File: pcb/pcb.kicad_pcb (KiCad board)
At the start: 2 copper layers, 62 parts, among them CN10 1x2, CN11 1x6, CN2 1x8, CN3 1x8, CN4 1x8, CN7 1x2, CN9 2x5, IC1 AP2112K-3.3TRG1, IC2 STM32f103C8T, IC4 AP62300TWU-7, SW1 switch_3x4, SW2 switch_3x4

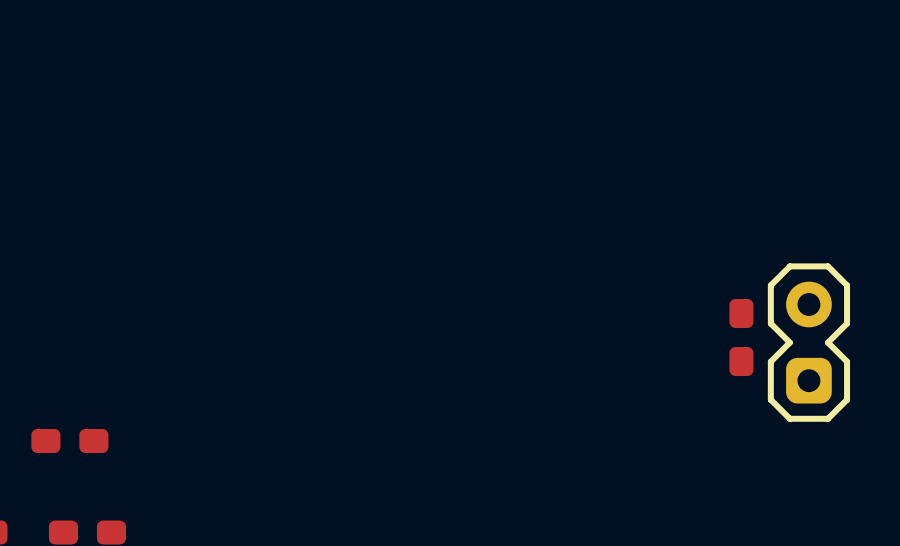
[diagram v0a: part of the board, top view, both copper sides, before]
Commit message: fixed 5V being GND net
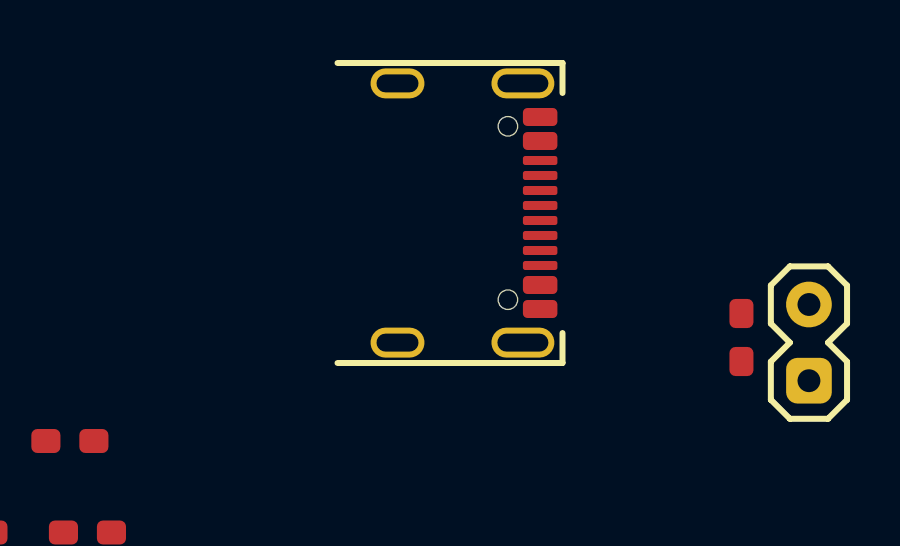
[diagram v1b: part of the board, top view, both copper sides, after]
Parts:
- added CN8: ~, USB:USB4105-GF-A, F.Cu at (121.3, 85.8)
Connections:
- C1 pad 1: GND -> 5V
- C24 pad 1: GND -> 5V
- C4 pad 1: GND -> 5V
- C5 pad 1: GND -> 5V
- C6 pad 1: GND -> 5V
- CN7 pad 1: GND -> 5V
- IC1 pad 1: GND -> 5V
- IC1 pad 3: GND -> 5V
- R8 pad 2: GND -> 5V
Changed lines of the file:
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@@
   (net 62 "unconnected-(CN9-Pad7)")
   (net 63 "/CAN_L")
+  (net 64 "5V")
+  (net 65 "unconnected-(CN8-SBU1-PadA8)")
+  (net 66 "unconnected-(CN8-SBU2-PadB8)")
   (footprint "pin_headers:1x2" (layer "F.Cu")
     (at 135 88.9 180)
@@
       (stroke (width 0.2) (type solid)) (layer "F.SilkS"))
     (pad "1" thru_hole roundrect (at 0 -2.54 90) (size 1.524 1.524) (drill 0.762) (layers "*.Cu" "*.Mask") (roundrect_rratio 0.25)
-      (net 1 "GND") (pintype "bidirectional"))
+      (net 64 "5V") (pintype "bidirectional"))
     (pad "2" thru_hole circle (at 0 0 90) (size 1.524 1.524) (drill 0.762) (layers "*.Cu" "*.Mask")
       (net 61 "/Servo VCC") (pintype "bidirectional"))
@@
       (net 4 "Net-(IC4-FB)") (pintype "bidirectional"))
     (pad "2" smd roundrect (at 0.8 0 180) (size 0.97 0.8) (layers "F.Cu" "F.Paste" "F.Mask") (roundrect_rratio 0.25)
-      (net 1 "GND") (pintype "bidirectional"))
+      (net 64 "5V") (pintype "bidirectional"))
   )
   (footprint "SMT:0603" (layer "F.Cu")
@@
       (stroke (width 0.2) (type solid)) (layer "F.Fab"))
     (pad "1" smd roundrect (at -0.8 0 90) (size 0.97 0.8) (layers "F.Cu" "F.Paste" "F.Mask") (roundrect_rratio 0.25)
-      (net 1 "GND") (pintype "bidirectional"))
+      (net 64 "5V") (pintype "bidirectional"))
     (pad "2" smd roundrect (at 0.8 0 90) (size 0.97 0.8) (layers "F.Cu" "F.Paste" "F.Mask") (roundrect_rratio 0.25)
       (net 1 "GND") (pintype "bidirectional"))
@@
       (net 1 "GND") (pintype "bidirectional"))
   )
+  (footprint "USB:USB4105-GF-A" (layer "F.Cu")
+    (at 121.285 85.85 -90)
+    (property "Digi-Key" "2073-USB4105-GF-ACT-ND")
+    (property "MPN" "USB4105-GF-A")
+    (property "Sheetfile" "pcb.kicad_sch")
+    (property "Sheetname" "")
+    (property "ki_description" "USB-C (USB TYPE-C) USB 2.0 Receptacle Connector 24 (16+8 Dummy) Position Surface Mount, Right Angle; Through Hole")
+    (property "ki_keywords" "USB-C type-c")
+    (attr smd)
+    (fp_text reference "CN8" (at 0 -0.5 -90 unlocked) (layer "F.Fab") hide
+        (effects (font (size 1 1) (thickness 0.1)))
+    )
+    (fp_text value "~" (at 0 -2 -90 unlocked) (layer "F.Fab") hide
+        (effects (font (size 1 1) (thickness 0.15)))
+    )
+    (fp_text user "${REFERENCE}" (at 0 -1 -90 unlocked) (layer "F.Fab")
+        (effects (font (size 1 1) (thickness 0.15)))
+    )
+    (fp_line (start -5 -5.5) (end -5 2)
+      (stroke (width 0.2) (type default)) (layer "F.SilkS"))
+    (fp_line (start -4 -5.5) (end -5 -5.5)
+      (stroke (width 0.2) (type default)) (layer "F.SilkS"))
+    (fp_line (start 5 -5.5) (end 4 -5.5)
+      (stroke (width 0.2) (type default)) (layer "F.SilkS"))
+    (fp_line (start 5 2) (end 5 -5.5)
+      (stroke (width 0.2) (type default)) (layer "F.SilkS"))
+    (fp_line (start -4.5 2.6) (end -4.5 -4.75)
+      (stroke (width 0.2) (type default)) (layer "F.Fab"))
+    (fp_line (start 4.5 -4.75) (end -4.5 -4.75)
+      (stroke (width 0.2) (type default)) (layer "F.Fab"))
+    (fp_line (start 4.5 2.6) (end -4.5 2.6)
+      (stroke (width 0.2) (type default)) (layer "F.Fab"))
+    (fp_line (start 4.5 2.6) (end 4.5 -4.75)
+      (stroke (width 0.2) (type default)) (layer "F.Fab"))
+    (pad "" np_thru_hole circle (at -2.89 -3.68 270) (size 0.56 0.56) (drill 0.65) (layers "F&B.Cu" "*.Mask"))
+    (pad "" np_thru_hole circle (at 2.89 -3.68 270) (size 0.56 0.56) (drill 0.65) (layers "F&B.Cu" "*.Mask"))
+    (pad "A1" smd roundrect (at -3.2 -4.755 270) (size 0.6 1.15) (layers "F.Cu" "F.Paste" "F.Mask") (roundrect_rratio 0.25)
+      (net 1 "GND") (pinfunction "GND") (pintype "power_out") (thermal_bridge_angle 45))
+    (pad "A4" smd roundrect (at -2.4 -4.755 270) (size 0.6 1.15) (layers "F.Cu" "F.Paste" "F.Mask") (roundrect_rratio 0.25)
+      (net 64 "5V") (pinfunction "VBUS") (pintype "power_in") (thermal_bridge_angle 45))
+    (pad "A5" smd roundrect (at -1.25 -4.755 270) (size 0.3 1.15) (layers "F.Cu" "F.Paste" "F.Mask") (roundrect_rratio 0.25)
+      (net 27 "Net-(CN8-CC1)") (pinfunction "CC1") (pintype "bidirectional") (thermal_bridge_angle 45))
+    (pad "A6" smd roundrect (at -0.25 -4.755 270) (size 0.3 1.15) (layers "F.Cu" "F.Paste" "F.Mask") (roundrect_rratio 0.25)
+      (net 52 "/MCU/USB_P") (pinfunction "D1P") (pintype "bidirectional") (thermal_bridge_angle 45))
+    (pad "A7" smd roundrect (at 0.25 -4.755 270) (size 0.3 1.15) (layers "F.Cu" "F.Paste" "F.Mask") (roundrect_rratio 0.25)
+      (net 51 "/MCU/USB_M") (pinfunction "D1N") (pintype "bidirectional") (thermal_bridge_angle 45))
+    (pad "A8" smd roundrect (at 1.25 -4.755 270) (size 0.3 1.15) (layers "F.Cu" "F.Paste" "F.Mask") (roundrect_rratio 0.25)
+      (net 65 "unconnected-(CN8-SBU1-PadA8)") (pinfunction "SBU1") (pintype "bidirectional") (thermal_bridge_angle 45))
+    (pad "B1" smd roundrect (at 3.2 -4.755 270) (size 0.6 1.15) (layers "F.Cu" "F.Paste" "F.Mask") (roundrect_rratio 0.25)
+      (net 1 "GND") (pinfunction "GND") (pintype "power_out") (thermal_bridge_angle 45))
+    (pad "B4" smd roundrect (at 2.4 -4.755 270) (size 0.6 1.15) (layers "F.Cu" "F.Paste" "F.Mask") (roundrect_rratio 0.25)
+      (net 64 "5V") (pinfunction "VBUS") (pintype "power_in") (thermal_bridge_angle 45))
+    (pad "B5" smd roundrect (at 1.75 -4.755 270) (size 0.3 1.15) (layers "F.Cu" "F.Paste" "F.Mask") (roundrect_rratio 0.25)
+      (net 26 "Net-(CN8-CC2)") (pinfunction "CC2") (pintype "bidirectional") (thermal_bridge_angle 45))
+    (pad "B6" smd roundrect (at 0.75 -4.755 270) (size 0.3 1.15) (layers "F.Cu" "F.Paste" "F.Mask") (roundrect_rratio 0.25)
+      (net 52 "/MCU/USB_P") (pinfunction "DP2") (pintype "bidirectional") (thermal_bridge_angle 45))
+    (pad "B7" smd roundrect (at -0.75 -4.755 270) (size 0.3 1.15) (layers "F.Cu" "F.Paste" "F.Mask") (roundrect_rratio 0.25)
+      (net 51 "/MCU/USB_M") (pinfunction "DN2") (pintype "bidirectional") (thermal_bridge_angle 45))
+    (pad "B8" smd roundrect (at -1.75 -4.755 270) (size 0.3 1.15) (layers "F.Cu" "F.Paste" "F.Mask") (roundrect_rratio 0.25)
+      (net 66 "unconnected-(CN8-SBU2-PadB8)") (pinfunction "SBU2") (pintype "bidirectional") (thermal_bridge_angle 45))
+    (pad "S1" thru_hole oval (at -4.32 0 270) (size 1 1.8) (drill oval 0.6 1.4) (layers "*.Cu" "*.Mask")
+      (net 1 "GND") (pinfunction "SHLD") (pintype "power_out") (thermal_bridge_angle 45))
+    (pad "S2" thru_hole oval (at 4.32 0 270) (size 1 1.8) (drill oval 0.6 1.4) (layers "*.Cu" "*.Mask")
+      (net 1 "GND") (pinfunction "SHLD") (pintype "power_out") (thermal_bridge_angle 45))
+    (pad "S3" thru_hole oval (at -4.32 -4.18 270) (size 1 2.1) (drill oval 0.6 1.7) (layers "*.Cu" "*.Mask")
+      (net 1 "GND") (pinfunction "SHLD") (pintype "power_out") (thermal_bridge_angle 45))
+    (pad "S4" thru_hole oval (at 4.32 -4.18 270) (size 1 2.1) (drill oval 0.6 1.7) (layers "*.Cu" "*.Mask")
+      (net 1 "GND") (pinfunction "SHLD") (pintype "power_out") (thermal_bridge_angle 45))
+    (model "/home/netl/projects/kicad-library/3d/USB4105-GF-A.stp"
+      (offset (xyz 0 -2.5 0))
+      (scale (xyz 1 1 1))
+      (rotate (xyz -90 0 0))
+    )
+  )
   (footprint "SMT:0603" (layer "F.Cu")
     (at 107 96.5)
@@
       (stroke (width 0.2) (type solid)) (layer "F.Fab"))
     (pad "1" smd roundrect (at -1.2 -0.95 90) (size 1.4 0.7) (layers "F.Cu" "F.Paste" "F.Mask") (roundrect_rratio 0.25)
-      (net 1 "GND") (pinfunction "VIN") (pintype "power_in"))
+      (net 64 "5V") (pinfunction "VIN") (pintype "power_in"))
     (pad "2" smd roundrect (at -1.2 0 90) (size 1.4 0.7) (layers "F.Cu" "F.Paste" "F.Mask") (roundrect_rratio 0.25)
       (net 1 "GND") (pinfunction "GND") (pintype "power_out"))
     (pad "3" smd roundrect (at -1.2 0.95 90) (size 1.4 0.7) (layers "F.Cu" "F.Paste" "F.Mask") (roundrect_rratio 0.25)
-      (net 1 "GND") (pinfunction "EN") (pintype "input"))
+      (net 64 "5V") (pinfunction "EN") (pintype "input"))
     (pad "4" smd roundrect (at 1.2 0.95 90) (size 1.4 0.7) (layers "F.Cu" "F.Paste" "F.Mask") (roundrect_rratio 0.25))
     (pad "5" smd roundrect (at 1.2 -0.95 90) (size 1.4 0.7) (layers "F.Cu" "F.Paste" "F.Mask") (roundrect_rratio 0.25)
@@
       (stroke (width 0.2) (type solid)) (layer "F.Fab"))
     (pad "1" smd roundrect (at -0.8 0) (size 0.97 0.8) (layers "F.Cu" "F.Paste" "F.Mask") (roundrect_rratio 0.25)
-      (net 1 "GND") (pintype "bidirectional"))
+      (net 64 "5V") (pintype "bidirectional"))
     (pad "2" smd roundrect (at 0.8 0) (size 0.97 0.8) (layers "F.Cu" "F.Paste" "F.Mask") (roundrect_rratio 0.25)
       (net 1 "GND") (pintype "bidirectional"))
@@
       (stroke (width 0.2) (type solid)) (layer "F.Fab"))
     (pad "1" smd roundrect (at -0.8 0 90) (size 0.97 0.8) (layers "F.Cu" "F.Paste" "F.Mask") (roundrect_rratio 0.25)
-      (net 1 "GND") (pintype "bidirectional"))
+      (net 64 "5V") (pintype "bidirectional"))
     (pad "2" smd roundrect (at 0.8 0 90) (size 0.97 0.8) (layers "F.Cu" "F.Paste" "F.Mask") (roundrect_rratio 0.25)
       (net 1 "GND") (pintype "bidirectional"))
@@
       (stroke (width 0.2) (type solid)) (layer "F.Fab"))
     (pad "1" smd roundrect (at -0.8 0) (size 0.97 0.8) (layers "F.Cu" "F.Paste" "F.Mask") (roundrect_rratio 0.25)
-      (net 1 "GND") (pintype "bidirectional"))
+      (net 64 "5V") (pintype "bidirectional"))
     (pad "2" smd roundrect (at 0.8 0) (size 0.97 0.8) (layers "F.Cu" "F.Paste" "F.Mask") (roundrect_rratio 0.25)
       (net 1 "GND") (pintype "bidirectional"))
@@
       (stroke (width 0.2) (type solid)) (layer "F.Fab"))
     (pad "1" smd roundrect (at -0.8 0) (size 0.97 0.8) (layers "F.Cu" "F.Paste" "F.Mask") (roundrect_rratio 0.25)
-      (net 1 "GND") (pintype "bidirectional"))
+      (net 64 "5V") (pintype "bidirectional"))
     (pad "2" smd roundrect (at 0.8 0) (size 0.97 0.8) (layers "F.Cu" "F.Paste" "F.Mask") (roundrect_rratio 0.25)
       (net 4 "Net-(IC4-FB)") (pintype "bidirectional"))

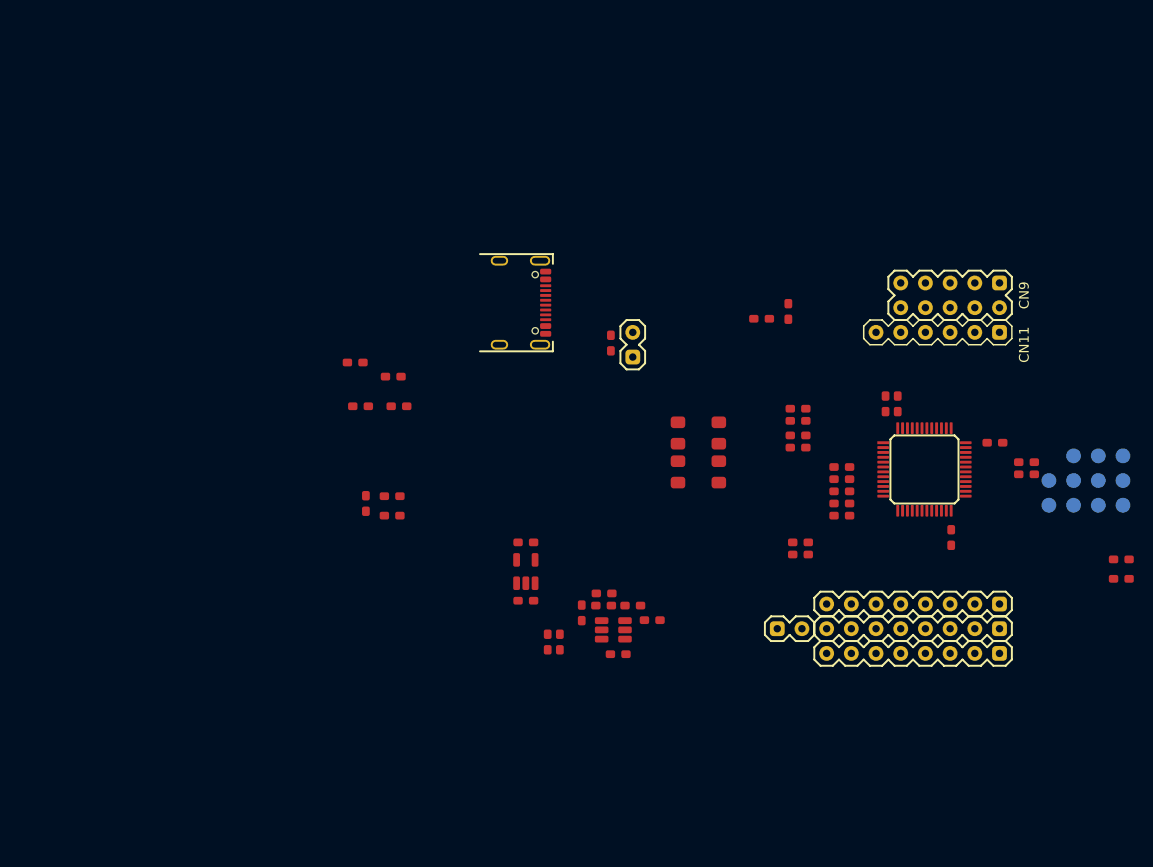
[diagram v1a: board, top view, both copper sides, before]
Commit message: added can+pwr header, worked layout
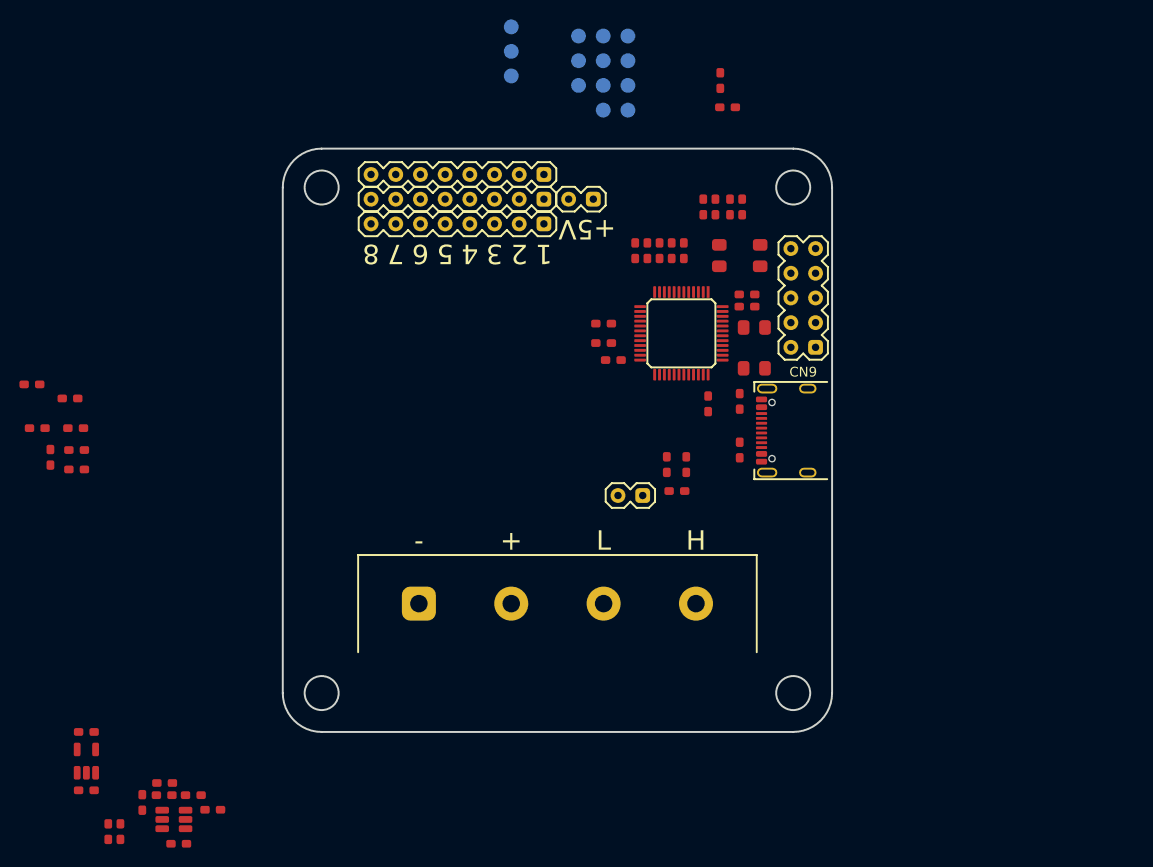
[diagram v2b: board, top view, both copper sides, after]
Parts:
- removed CN11: 1x6, pin_headers:1x6
- added CN5: 1x4, connectors:YK4410403000G, F.Cu at (127.2, 116.8)
- added TP12: test_point, PCB:test_point, B.Cu at (122.5, 62.5)
- added TP13: test_point, PCB:test_point, B.Cu at (122.5, 60.0)
- added TP14: test_point, PCB:test_point, B.Cu at (122.5, 57.5)
- moved TP6 70.7 mm to (129.4, 58.4), turned to -90 degrees
- moved TP3 70.3 mm to (132.0, 58.4), turned to -90 degrees
- moved TP4 70.2 mm to (134.5, 58.4), turned to -90 degrees
- moved CN4 68.0 mm to (118.2, 72.7)
- moved TP1 67.2 mm to (129.4, 61.0), turned to -90 degrees
- moved TP7 66.8 mm to (132.0, 61.0), turned to -90 degrees
- moved TP8 66.6 mm to (134.5, 61.0), turned to -90 degrees
- moved CN3 64.4 mm to (118.2, 75.2)
- moved TP5 63.6 mm to (129.4, 63.5), turned to -90 degrees
- moved TP2 63.2 mm to (132.0, 63.5), turned to -90 degrees
- moved TP11 63.0 mm to (134.5, 63.5), turned to -90 degrees
- moved CN2 61.0 mm to (118.2, 77.7)
- moved TP9 59.6 mm to (132.0, 66.0), turned to -90 degrees
- moved TP10 59.4 mm to (134.5, 66.0), turned to -90 degrees
- moved CN7 50.3 mm to (128.4, 75.2), turned to -90 degrees
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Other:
- board outline added: 56.5 x 60 mm
- board text added: "+"
- board text added: "+5V"
- board text added: "-"
- board text added: "1"
- board text added: "2"
- board text added: "3"
- board text added: "4"
- board text added: "5"
- board text added: "6"
- board text added: "7"
- board text added: "8"
- board text added: "CAN bus"
- board text added: "H"
- board text added: "L"
- board text added: "battery monitor"
- board text added: "power supply"

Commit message: added DIP switches, footprints
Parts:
- added IC3: INA199B2, sc70:SC70-6L, F.Cu at (82.5, 99.5)
- added IC5: MCP2551, SOP:SO-8, F.Cu at (142.0, 105.5)
- added SW3: 219-3LPST, buttons:219-3LPST, F.Cu at (121.0, 89.0)
- moved C24 8.54 mm to (146.5, 105.5), turned to -90 degrees
- moved R15 7.38 mm to (137.0, 109.0)
- moved R14 3.07 mm to (136.8, 106.5)
- moved CN10 1.76 mm to (134.0, 104.0), turned to 180 degrees
- renumbered TP9 to TP6, TP10 to TP7, TP11 to TP8
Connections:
- IC2 pad 21: Net-(IC2-PB10) -> /MCU/ADDR1
- IC2 pad 22: Net-(IC2-PB11) -> /MCU/ADDR2
- IC2 pad 25: Net-(IC2-PB12) -> /MCU/ADDR3

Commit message: updated components. worked on layout
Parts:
- removed C8, C9: 100n, SMT:0603
- added C25: 100n, SMT:0603, F.Cu at (132.2, 117.1)
- added CN6: 1x2, connectors:XT60, F.Cu at (115.4, 114.5)
- added F1: F, connectors:3557-15, F.Cu at (123.0, 118.0)
- added L1: 3u3, inductor:5x5, F.Cu at (134.0, 106.0)
- added R7: 750uR, SMT:2512-high-current, F.Cu at (133.0, 126.0)
- moved SW2 77.4 mm to (78.1, 118.1), turned to 0 degrees
- moved SW1 75.4 mm to (80.0, 124.0), turned to 0 degrees
- moved C22 67.7 mm to (131.5, 134.0), turned to -90 degrees
- moved CN9 65.7 mm to (89.8, 105.1)
- moved C4 65.6 mm to (139.0, 109.5), turned to -90 degrees
- moved R11 65.6 mm to (133.0, 134.0), turned to -90 degrees
- moved C1 65.4 mm to (134.0, 101.0)
- moved C2 65.4 mm to (134.0, 95.0)
- moved IC1 65.4 mm to (134.0, 98.0)
- moved R5 64.9 mm to (134.2, 116.6)
- moved C6 63.2 mm to (137.5, 109.5), turned to -90 degrees
- moved R6 61.3 mm to (134.2, 118.1), turned to 180 degrees
- moved C7 58.4 mm to (137.5, 112.5)
- moved C3 55.8 mm to (128.5, 118.0)
- moved R2 55.2 mm to (130.0, 121.0), turned to -90 degrees
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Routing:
- added copper zone on F.Cu, net /Battery
- added copper zone on F.Cu, net /power supply/+
- added copper zone on B.Cu, net GND
- added copper zone on F.Cu, net GND
- added copper zone on F.Cu, net Net-(CN6-Pad1)
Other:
- board size 56.5 x 60 mm -> 63 x 60 mm
- board text added: "3.3 V"
